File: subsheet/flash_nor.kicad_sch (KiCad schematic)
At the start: 2 parts, among them U1401 W25Q128JVS

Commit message: Silkscreen work. Edit tittle block/version number
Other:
- company: copyright Escape This 2024 -> (c) Vincent Dalstra
- title: Puzzle Board -> Untitled 4-layer JLCPCB
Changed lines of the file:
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@@
 	(paper "A5")
 	(title_block
-		(title "Puzzle Board")
-		(date "2024-03-20")
-		(rev "4.0.0")
-		(company "copyright Escape This 2024")
+		(title "Untitled 4-layer JLCPCB")
+		(date "2024-06-14")
+		(rev "1.0.0")
+		(company "(c) Vincent Dalstra")
 		(comment 1 "Drawn by: VGD")
 		(comment 2 "Check by:")

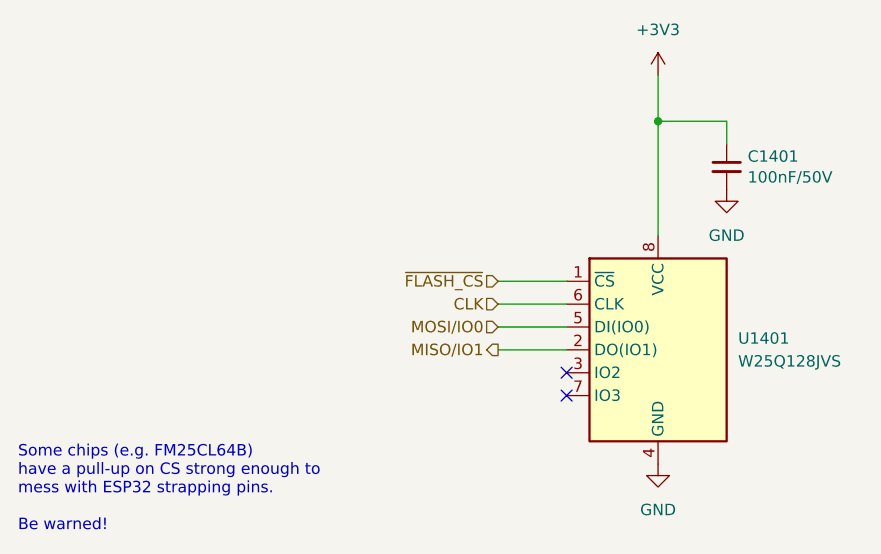
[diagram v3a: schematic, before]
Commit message: Move all subsheets into 'main' subsheet, below root
Keeping all the subsheets in a dedicated 'subsheet' folder makes things
much, much neater. However, specifying filepaths for subsheets has an
interesting problem; they use paths RELATIVE TO THE PARENT SHEET.

The consequence of is that if a subsheet is part of the root sheet, it
needs to be prefixed with 'subsheet/', but NOT if it's further down.
This inconsistency can be resolved by having a single 'main' sheet at
the top that doesn't move.

It's also useful to have a top-level space to put down changelogs,
descriptions etc.
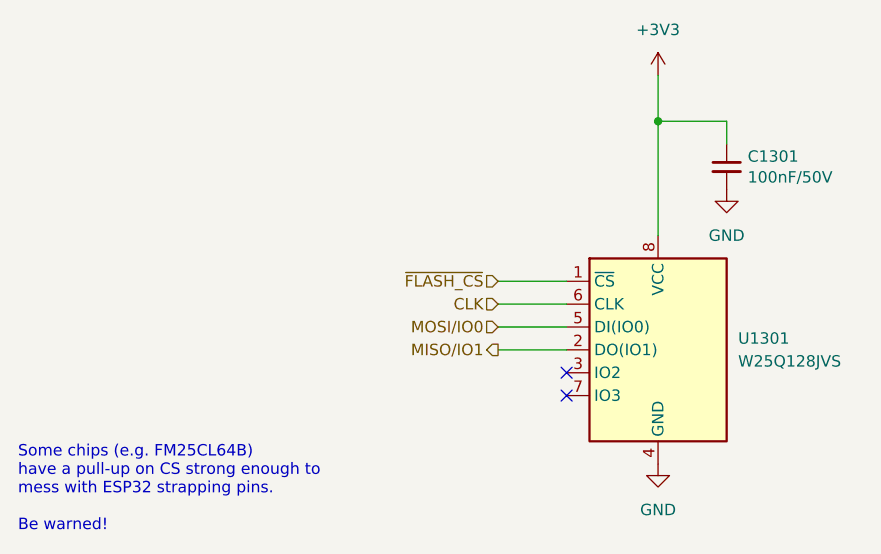
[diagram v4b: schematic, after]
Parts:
- renumbered C1401 to C1301, U1401 to U1301
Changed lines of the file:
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@@
 		(shape input)
 		(at 73.66 58.42 180)
-		(fields_autoplaced yes)
 		(effects
 			(font
@@
 		(shape output)
 		(at 73.66 60.96 180)
-		(fields_autoplaced yes)
 		(effects
 			(font
@@
 		(shape input)
 		(at 73.66 55.88 180)
-		(fields_autoplaced yes)
 		(effects
 			(font
@@
 		(shape input)
 		(at 73.66 53.34 180)
-		(fields_autoplaced yes)
 		(effects
 			(font
@@
 		(on_board yes)
 		(dnp no)
-		(property "Reference" "C1401"
+		(property "Reference" "C1301"
 			(at 101.3968 39.4716 0)
 			(effects
@@
 		(instances
 			(project "ESP_bare_chip_test_board"
-				(path "/45b6f84a-e69b-48be-a49b-bc68872e2c15/d37d0921-0af2-43fb-b20d-bf592b897b4a"
-					(reference "C1401")
+				(path "/45b6f84a-e69b-48be-a49b-bc68872e2c15/f48098a1-cacc-4192-b650-2a34a2ba76dc/96546e56-3235-4dd6-8398-850f11be4578"
+					(reference "C1301")
 					(unit 1)
 				)
@@
 		(dnp no)
 		(fields_autoplaced yes)
-		(property "Reference" "#PWR01401"
+		(property "Reference" "#PWR1301"
 			(at 91.44 34.29 0)
 			(effects
@@
 		(instances
 			(project "ESP_bare_chip_test_board"
-				(path "/45b6f84a-e69b-48be-a49b-bc68872e2c15/d37d0921-0af2-43fb-b20d-bf592b897b4a"
-					(reference "#PWR01401")
+				(path "/45b6f84a-e69b-48be-a49b-bc68872e2c15/f48098a1-cacc-4192-b650-2a34a2ba76dc/96546e56-3235-4dd6-8398-850f11be4578"
+					(reference "#PWR1301")
 					(unit 1)
 				)
@@
 		(dnp no)
 		(fields_autoplaced yes)
-		(property "Reference" "#PWR01402"
+		(property "Reference" "#PWR1302"
 			(at 91.44 80.01 0)
 			(effects
@@
 		(instances
 			(project "ESP_bare_chip_test_board"
-				(path "/45b6f84a-e69b-48be-a49b-bc68872e2c15/d37d0921-0af2-43fb-b20d-bf592b897b4a"
-					(reference "#PWR01402")
+				(path "/45b6f84a-e69b-48be-a49b-bc68872e2c15/f48098a1-cacc-4192-b650-2a34a2ba76dc/96546e56-3235-4dd6-8398-850f11be4578"
+					(reference "#PWR1302")
 					(unit 1)
 				)
@@
 		(dnp no)
 		(fields_autoplaced yes)
-		(property "Reference" "U1401"
+		(property "Reference" "U1301"
 			(at 100.33 59.69 0)
 			(effects
@@
 		(instances
 			(project "ESP_bare_chip_test_board"
-				(path "/45b6f84a-e69b-48be-a49b-bc68872e2c15/d37d0921-0af2-43fb-b20d-bf592b897b4a"
-					(reference "U1401")
+				(path "/45b6f84a-e69b-48be-a49b-bc68872e2c15/f48098a1-cacc-4192-b650-2a34a2ba76dc/96546e56-3235-4dd6-8398-850f11be4578"
+					(reference "U1301")
 					(unit 1)
 				)
@@
 		(dnp no)
 		(fields_autoplaced yes)
-		(property "Reference" "#PWR01403"
+		(property "Reference" "#PWR1303"
 			(at 99.06 49.53 0)
 			(effects
@@
 		(instances
 			(project "ESP_bare_chip_test_board"
-				(path "/45b6f84a-e69b-48be-a49b-bc68872e2c15/d37d0921-0af2-43fb-b20d-bf592b897b4a"
-					(reference "#PWR01403")
+				(path "/45b6f84a-e69b-48be-a49b-bc68872e2c15/f48098a1-cacc-4192-b650-2a34a2ba76dc/96546e56-3235-4dd6-8398-850f11be4578"
+					(reference "#PWR1303")
 					(unit 1)
 				)
